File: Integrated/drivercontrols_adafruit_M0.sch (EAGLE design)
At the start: 19 parts

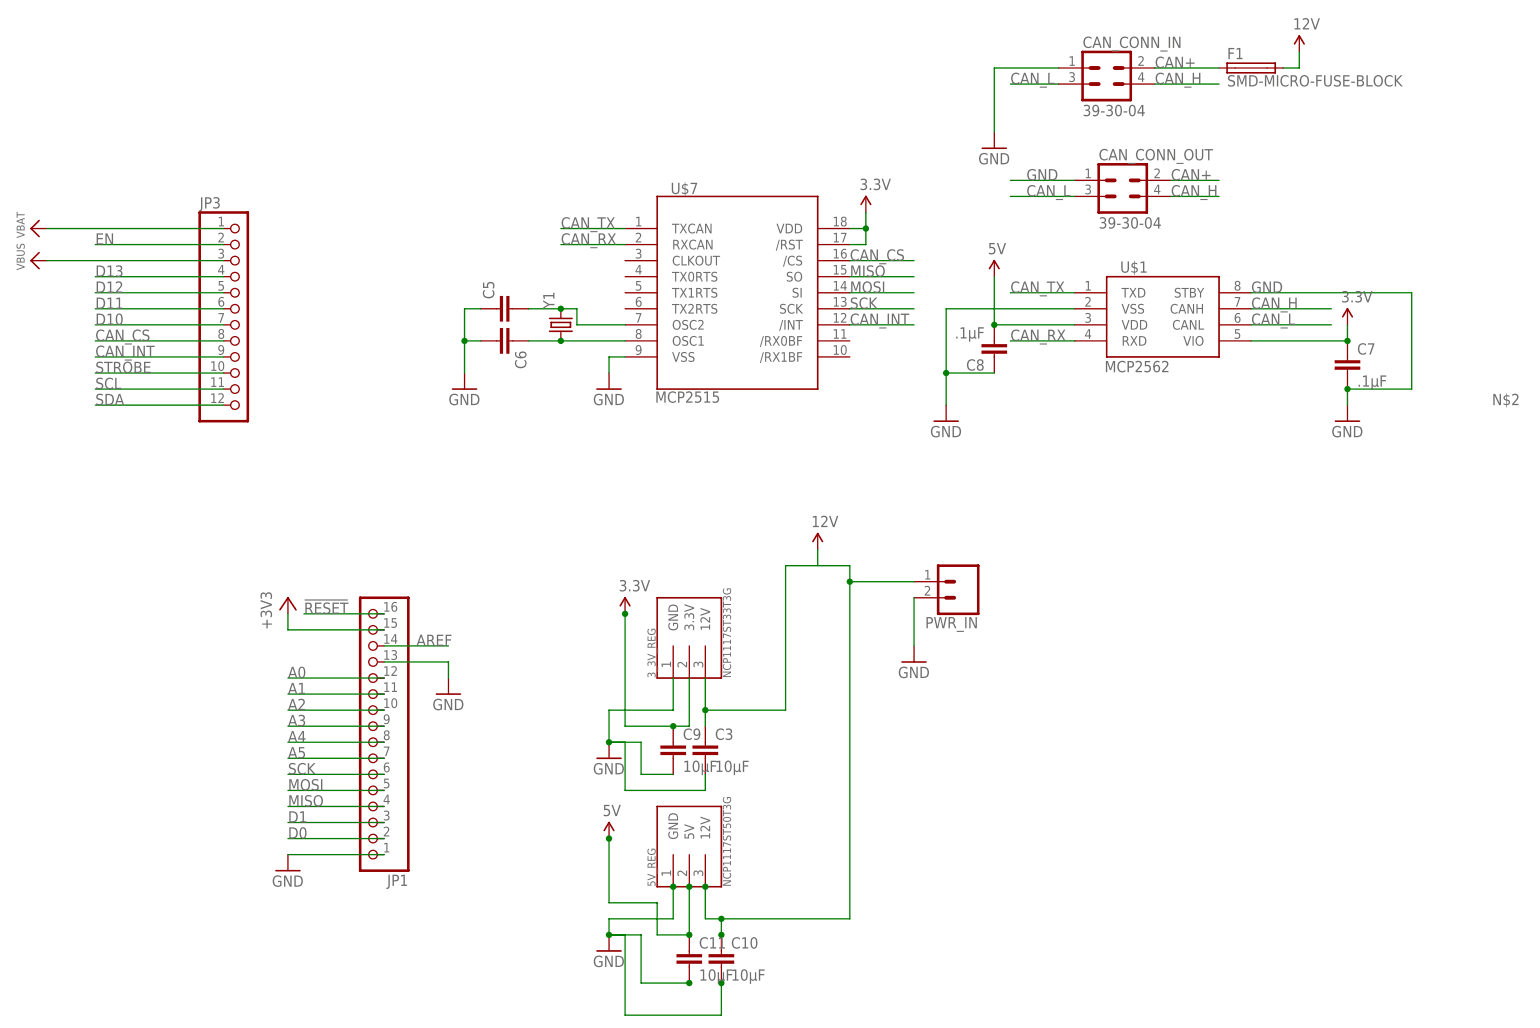
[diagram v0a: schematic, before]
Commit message: left side of integrated board
has the old driver control board with the m0 addalogger board
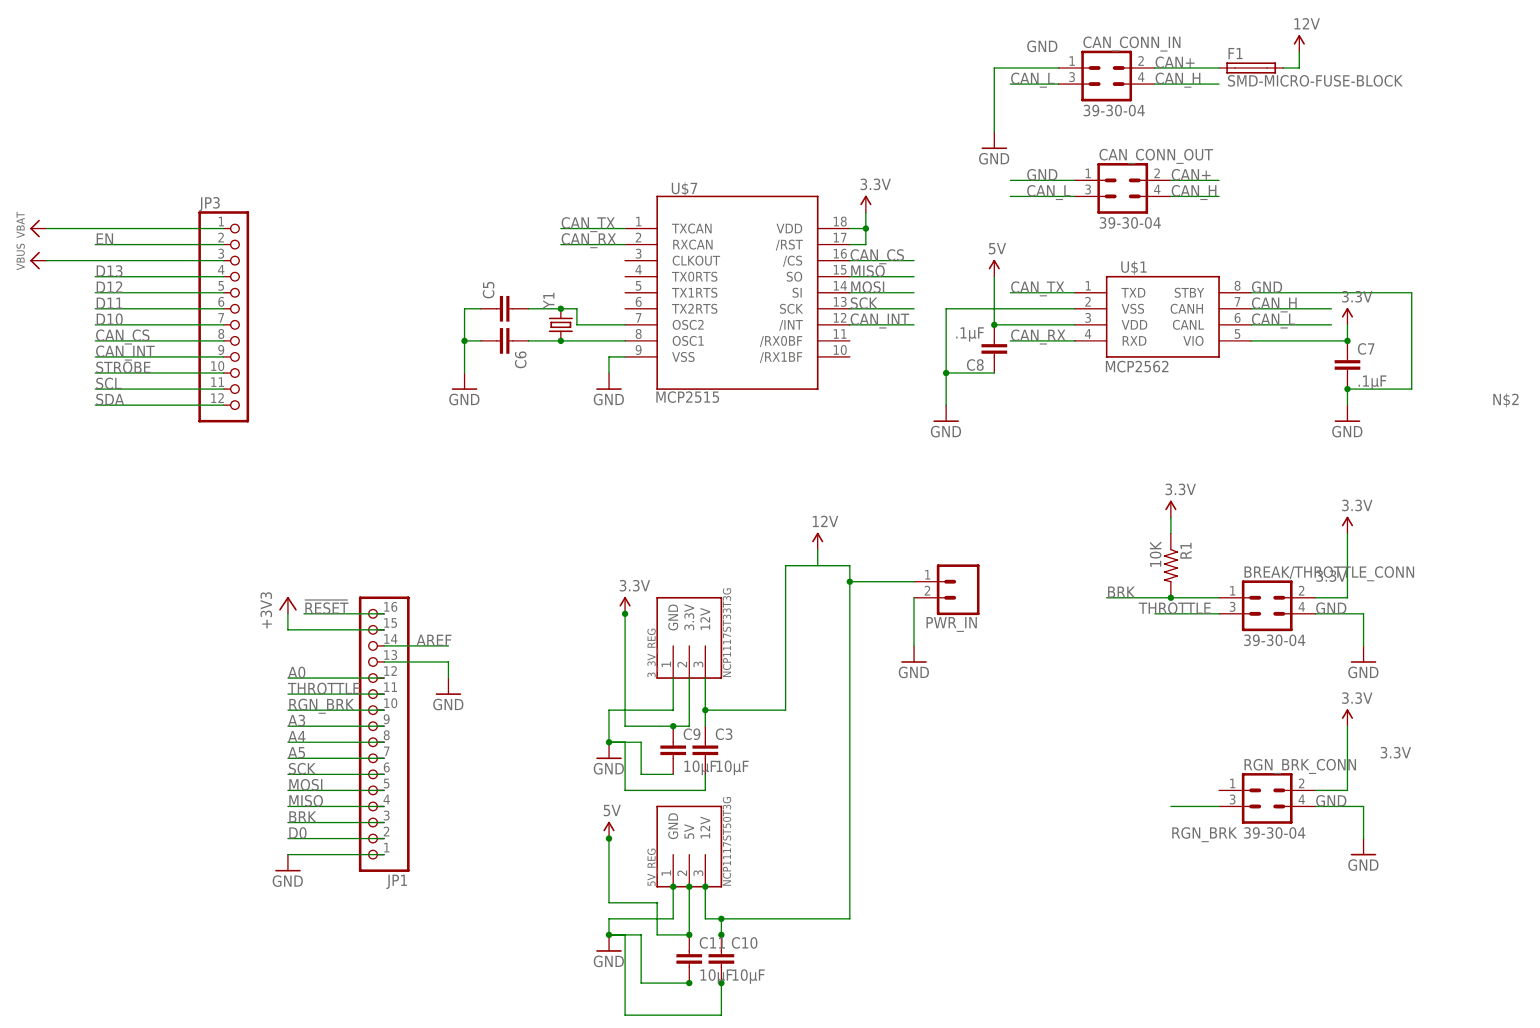
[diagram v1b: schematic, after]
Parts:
- added BREAK/THROTTLE_CONN, RGN_BRK_CONN: 39-30-04, con-molex-mini-fit:39-30-04
- added R1: 10K, BeagleBone_Black_Wireless:R-US_M0805
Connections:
- removed net A1: JP1.11
- removed net A2: JP1.10
- removed net D1: JP1.3
- new net BRK: BREAK/THROTTLE_CONN.1, JP1.3, R1.2
- new net RGN_BRK: JP1.10, RGN_BRK_CONN.3
- new net THROTTLE: BREAK/THROTTLE_CONN.3, JP1.11
- net 3.3V: now also BREAK/THROTTLE_CONN.2, R1.1, RGN_BRK_CONN.2
- net GND: now also BREAK/THROTTLE_CONN.4, RGN_BRK_CONN.4
